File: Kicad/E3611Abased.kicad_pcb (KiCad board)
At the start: 2 copper layers, 182 x 127 mm, 139 parts, among them IC1 LTC2487, IC2 LTC2617, IC3 TC74, J1 Conn_02x05_Odd_Even, J2 Conn_01x02, J3 Conn_01x02, J4 Conn_01x03, J5 Conn_01x04, J6 Conn_01x01, J7 Conn_01x01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

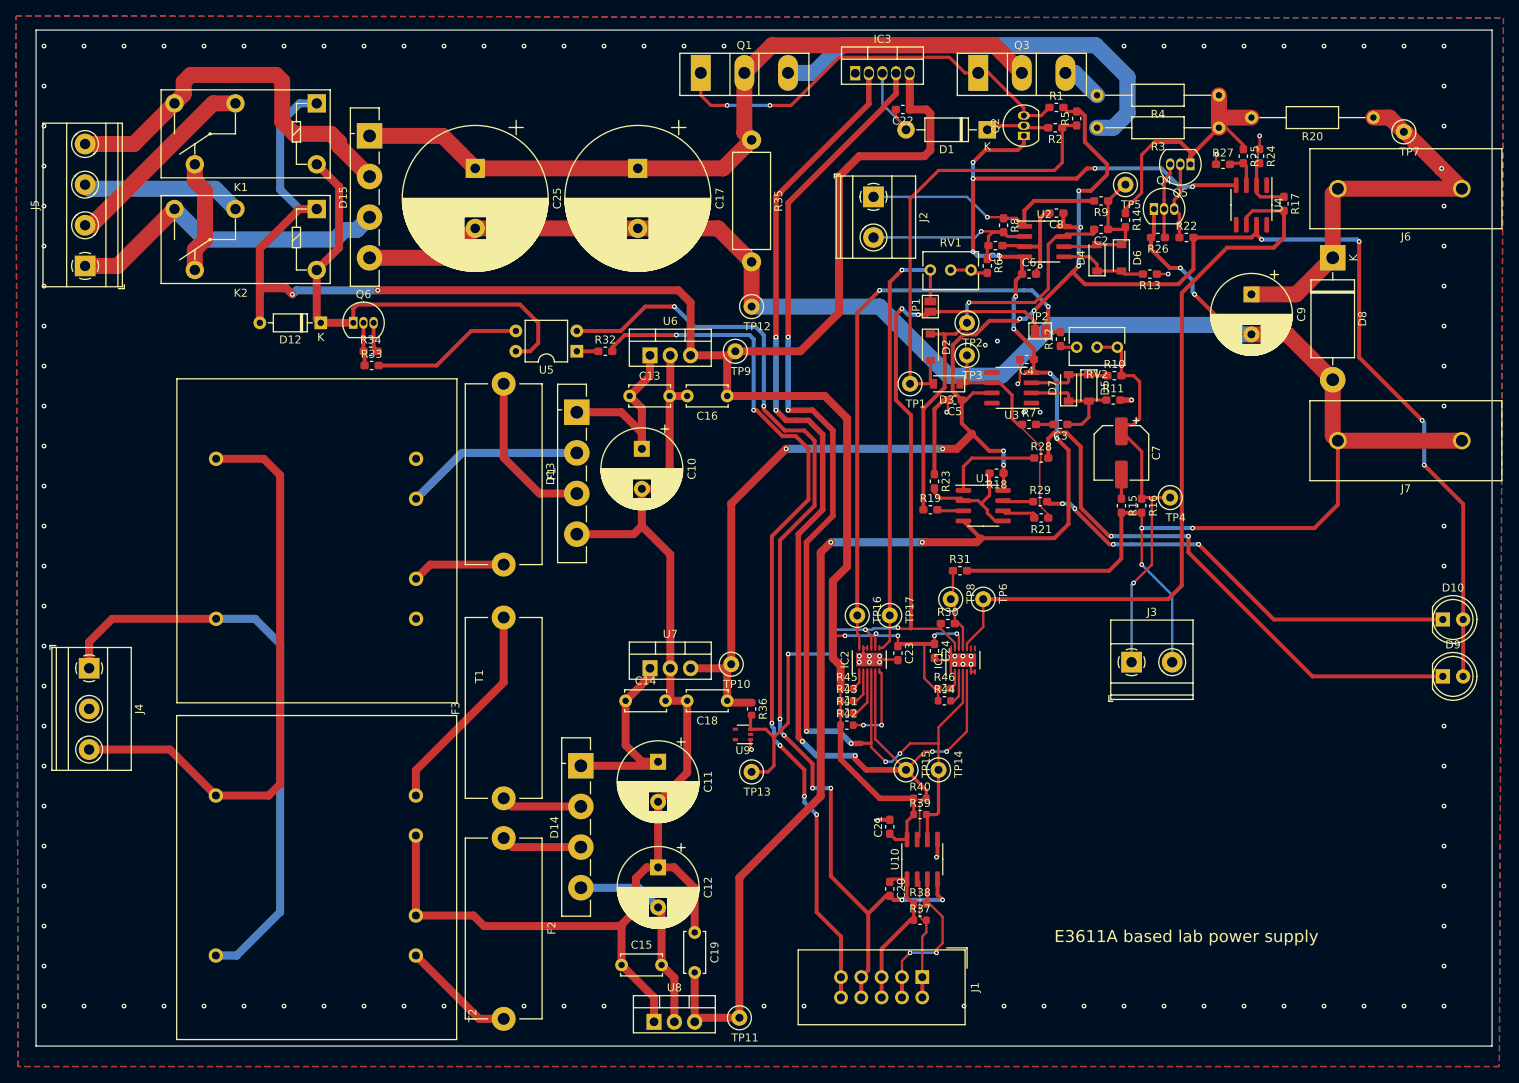
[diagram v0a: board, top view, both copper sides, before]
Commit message: fixed bugs in PCB, added frontpanel, added SW for frontpanel
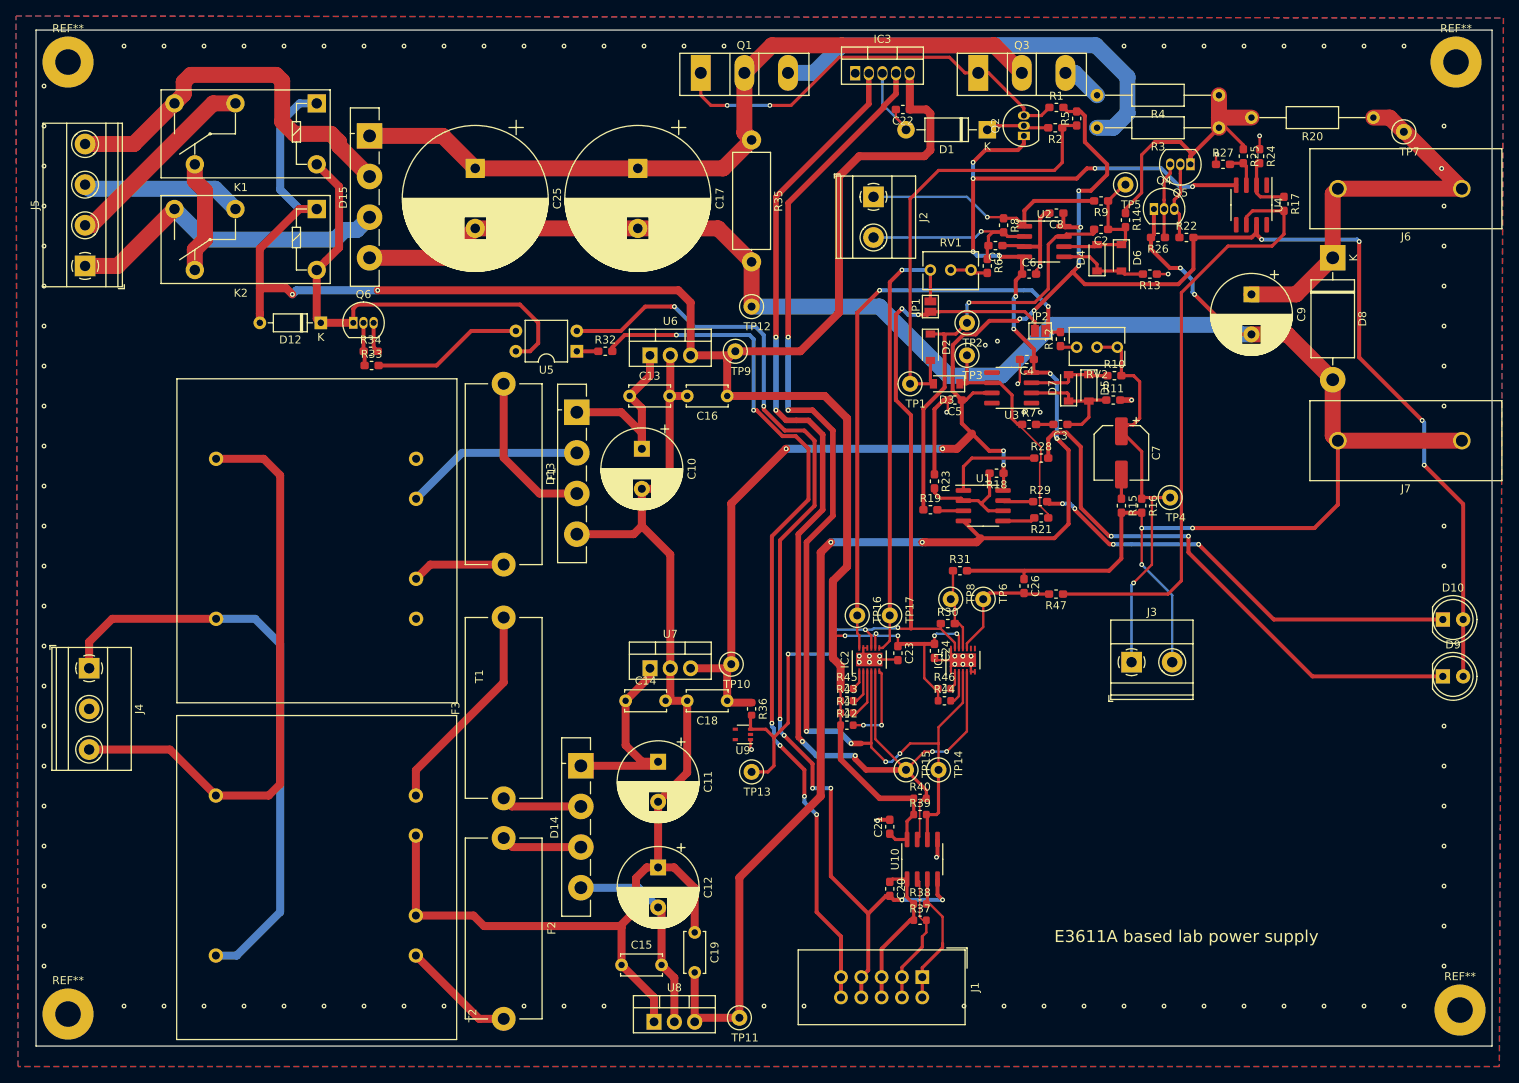
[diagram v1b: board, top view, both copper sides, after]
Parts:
- added C26: 100n, Capacitor_SMD:C_0603_1608Metric_Pad1.05x0.95mm_HandSolder, F.Cu at (157.5, 102.5)
- added R47: 1K, Resistor_SMD:R_0603_1608Metric_Pad1.05x0.95mm_HandSolder, F.Cu at (161.5, 103.5)
- added REF**: MountingHole_3.2mm_M3_Pad, MountingHole:MountingHole_3.2mm_M3_Pad, F.Cu at (211.5, 37.0)
- added REF**: MountingHole_3.2mm_M3_Pad, MountingHole:MountingHole_3.2mm_M3_Pad, F.Cu at (38.0, 37.0)
- added REF**: MountingHole_3.2mm_M3_Pad, MountingHole:MountingHole_3.2mm_M3_Pad, F.Cu at (38.0, 156.0)
- added REF**: MountingHole_3.2mm_M3_Pad, MountingHole:MountingHole_3.2mm_M3_Pad, F.Cu at (212.0, 155.5)
- R26: value 330R -> 680R
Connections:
- J1 pad 1: /Digital/IS_SDA -> /Digital/IS_SCL
- J1 pad 2: /Digital/IS_SDA -> /Digital/IS_SCL
- J1 pad 3: /Digital/IS_SCL -> /Digital/IS_SDA
- J1 pad 4: /Digital/IS_SCL -> /Digital/IS_SDA
- R17 pad 2: /Analog/CH2 -> Net-(R17-Pad2)
- U1 pad 5: Net-(R18-Pad2) -> Net-(R21-Pad2)
- U1 pad 6: Net-(R21-Pad2) -> Net-(R18-Pad2)
- U4 pad 6: /Analog/CH2 -> Net-(R17-Pad2)
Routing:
- net /Analog/CH2: track 94.1 -> 15.6 mm
- net Net-(R17-Pad2): track 0.00 -> 76.2 mm
- net /Digital/IS_SCL: track 20.0 -> 17.0 mm, vias 2 -> 0
- net GND: track 266.9 -> 268.0 mm
- net /Digital/IS_SDA: track 15.7 -> 16.8 mm
- net Net-(R18-Pad2): track 15.0 -> 14.3 mm
- net GNDREF: vias 123 -> 116
